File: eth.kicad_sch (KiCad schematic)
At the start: 32 parts, among them J3 Bus_RJ45_5-2337992-8, U10 LAN8742A-CZ-TR, U9 TPD4E05U06QDQARQ1, Y3 Oscillator_25MHz_ESC_2016MV

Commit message: [#95398] Implement basic post review sugestions
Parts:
- removed J3: Bus_RJ45_5-2337992-8, antmicro-footprints:RJ45_X-2337992-8_Horizontal, symbol antmicroModularConnectorsJacksWithMagnetics:Bus_RJ45_5-2337992-8
- removed R24: R_0R_0402, antmicro-footprints:R_0402_1005Metric, symbol antmicroResistors0402:R_0R_0402
- added FB2: FB_1k5Z_0.5A_Murata-BLM18HE_0603, antmicro-footprints:FB_0603_1608Metric, symbol antmicroFerriteBeadsandChips:FB_1k5Z_0.5A_Murata-BLM18HE_0603
- added J3: RJ45_Abracon_ARJM11B1-502-AB-EW2, antmicro-footprints:RJ45_ARJM11B1-502-AB-EW2_Horizontal, symbol antmicroModularConnectorsJacks:RJ45_Abracon_ARJM11B1-502-AB-EW2
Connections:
- net +3V3: now also R31.2, R32.2, R33.2, R34.2, R35.2, FB2.2
- net 3V3_ETH: now also FB2.1, J3.5, J3.6; no longer R31.2, R32.2, R33.2, R34.2, R35.2
- net LED1: now also J3.13 (LED_Y+)
- net LED2: now also J3.11 (LED_G+)
- net RXN: now also J3.4
- net RXP: now also J3.3
- net TXN: now also J3.2
- net TXP: now also J3.1
- net at R23.2: now also J3.14 (LED_Y-)
- net at R22.2: now also J3.12 (LED_G-)
- net at R40.2: now also J3.SH
- no-connect marks 9 -> 5
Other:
- note removed: "TODO should be pulled to MCU VDD but its the same voltage"
- moved on the sheet: C33, C34, R22, R23, R40, U9

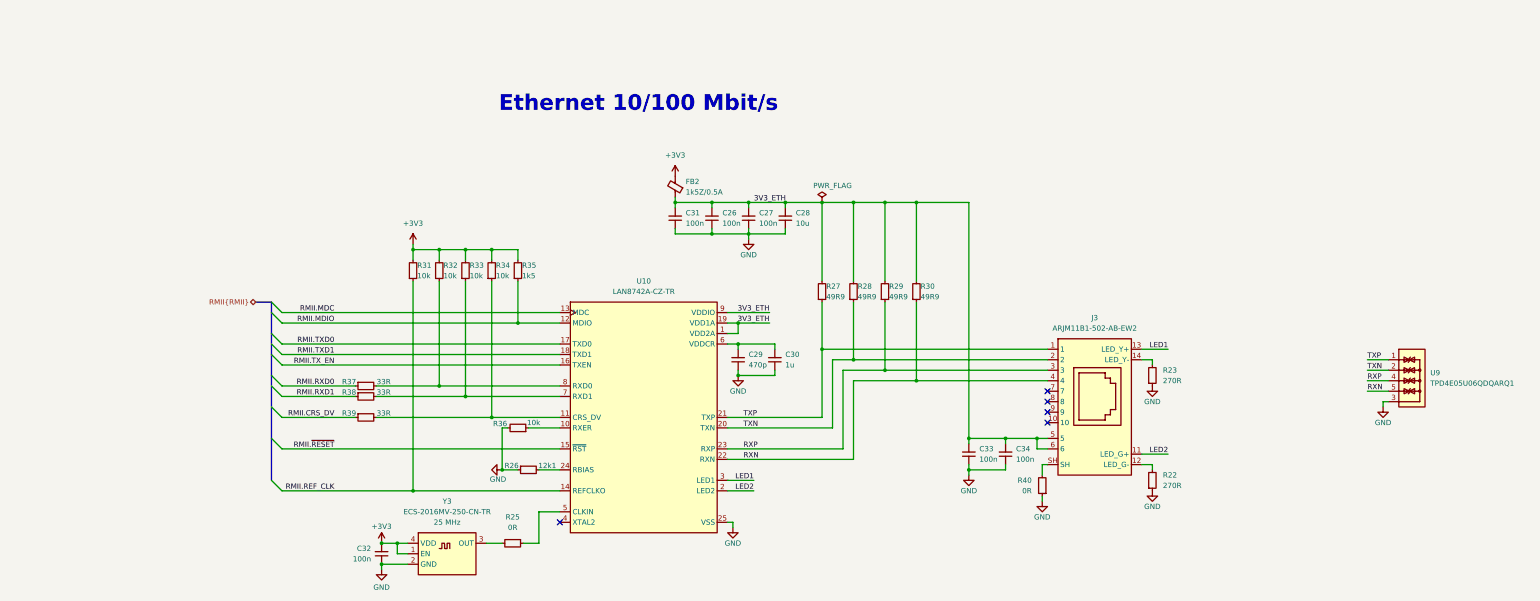
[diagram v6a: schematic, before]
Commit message: [#95398] Add markings for ETH strap resistors
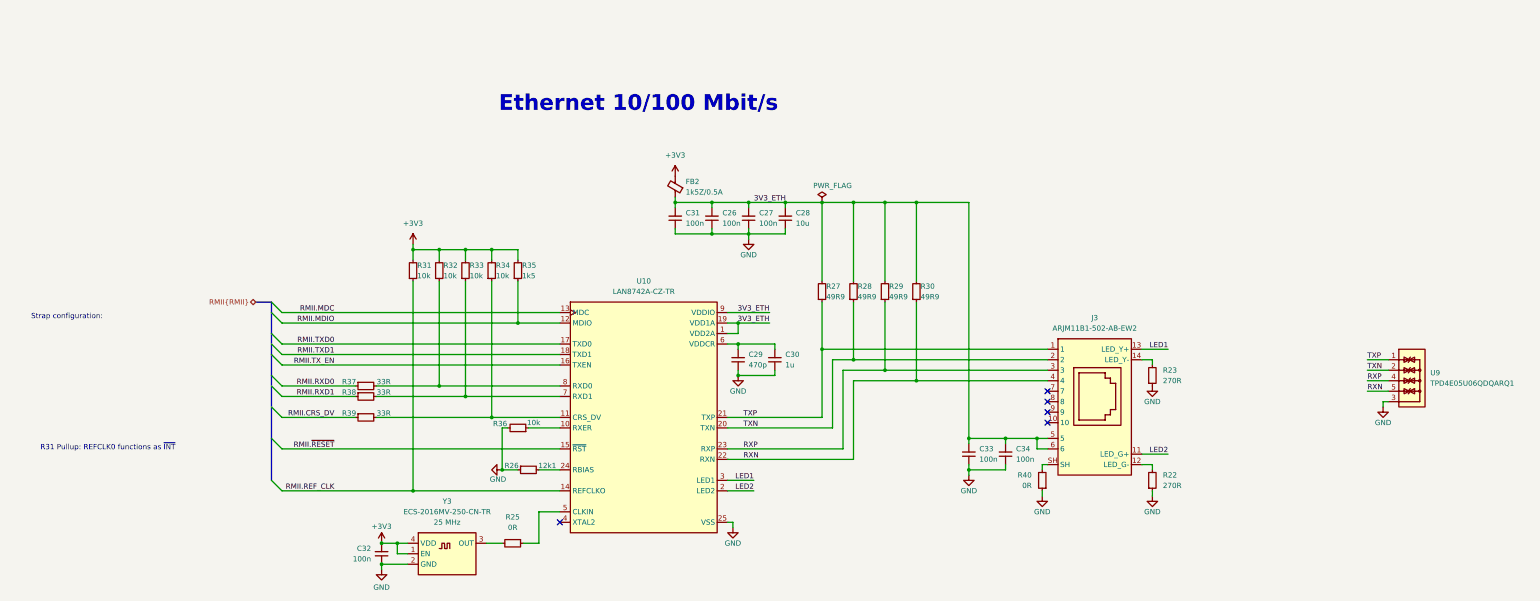
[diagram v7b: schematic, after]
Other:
- note added: "R31 Pullup: REFCLK0 functions as ~{INT}"
- note added: "Strap configuration:"
- title: renode-reference-platform -> STM32H7 Renode Reference Platform
- moved on the sheet: R40

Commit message: [#95451] Finalizing final placement
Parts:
- added C114, C115: C_100n_0402, antmicro-footprints:C_0402_1005Metric, symbol antmicroCapacitors0402:C_100n_0402
- added R7: R_0R_0402, antmicro-footprints:R_0402_1005Metric, symbol antmicroResistors0402:R_0R_0402
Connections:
- net GND: now also C114.1, C115.1, R7.1
- net at J3.SH, R40.2: now also C114.2, C115.2, R7.2
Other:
- moved on the sheet: R40
